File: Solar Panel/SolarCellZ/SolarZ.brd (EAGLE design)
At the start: 99 x 99 mm, 29 parts, among them X1 BU-SMA-V

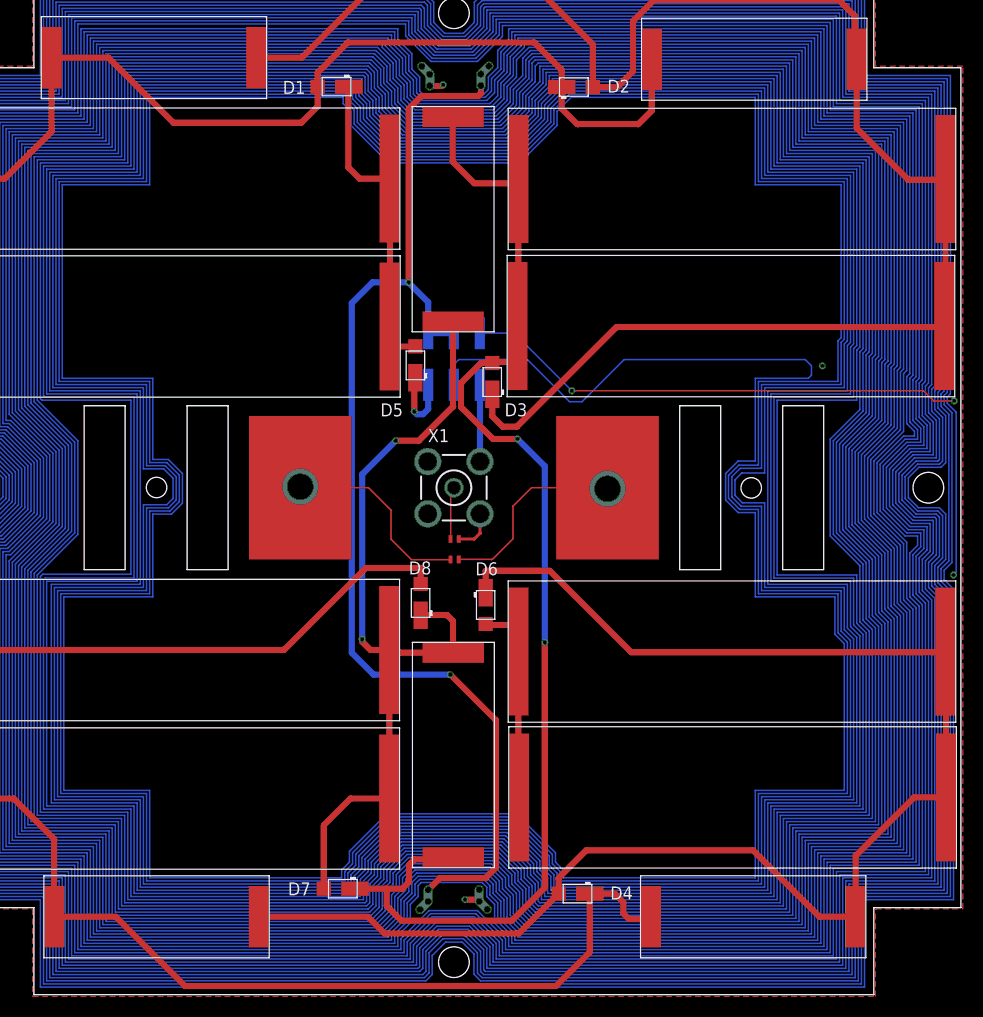
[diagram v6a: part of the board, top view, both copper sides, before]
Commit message: Solar Z Panel done passing all DFM checks
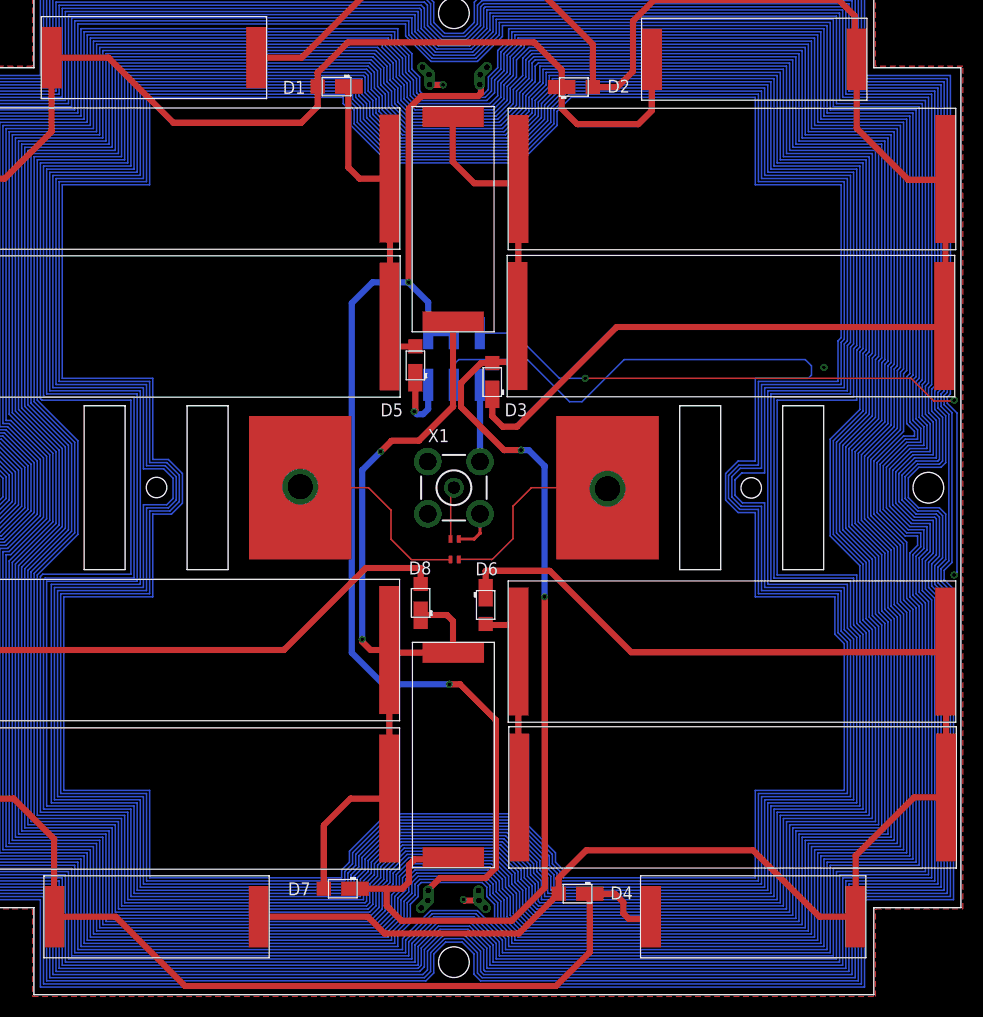
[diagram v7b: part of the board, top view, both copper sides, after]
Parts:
- moved F1 0.25 mm to (47.7, 6.25)
- moved F2 0.21 mm to (42.8, 84.3)
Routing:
- net N$8: track 41447.2 -> 41444.1 mm
- net GND: track 40.2 -> 39.6 mm
